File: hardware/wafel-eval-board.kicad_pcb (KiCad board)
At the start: 2 copper layers, 95 x 95 mm, 117 parts, among them U101 TPS70933, U102 LM5163DDA, U201 BQ769x2

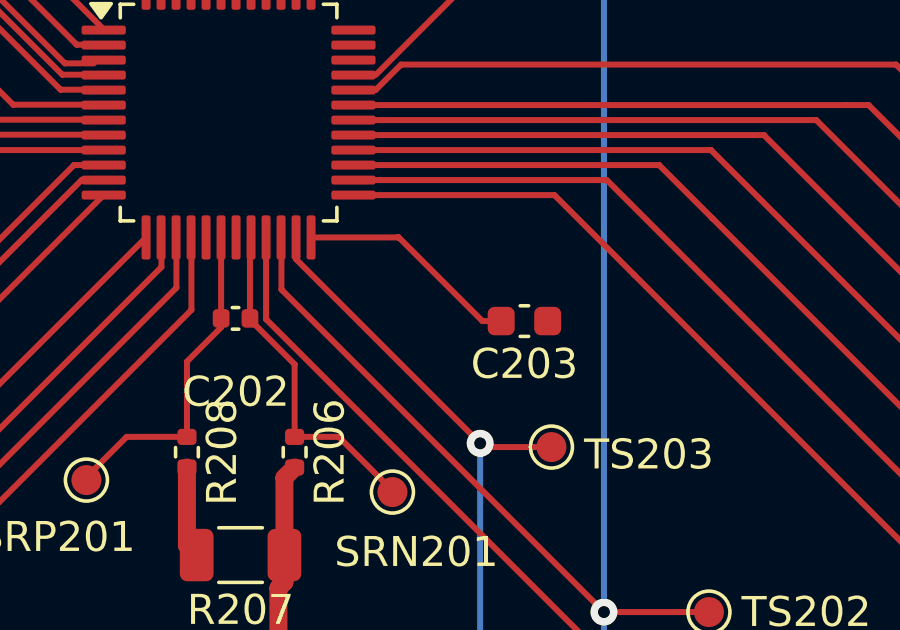
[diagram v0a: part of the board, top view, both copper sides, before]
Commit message: add sync folder
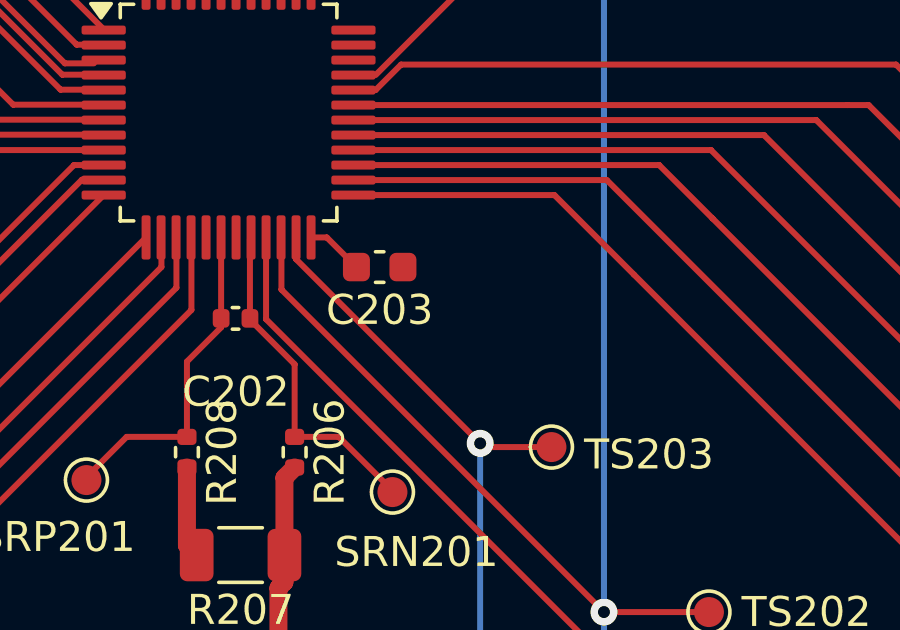
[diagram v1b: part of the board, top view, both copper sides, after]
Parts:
- moved C203 5.15 mm to (142.3, 93.0)
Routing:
- net Net-(U201-REG18): track 7.50 -> 1.92 mm
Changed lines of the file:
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@@
 	(footprint "Capacitor_SMD:C_0603_1608Metric"
 		(layer "F.Cu")
-		(at 147.1 94.8 180)
+		(at 142.275 93 180)
 		(descr "Capacitor SMD 0603 (1608 Metric), square (rectangular) end terminal, IPC-7351 nominal, (Body size source: IPC-SM-782 page 76, https://www.pcb-3d.com/wordpress/wp-content/uploads/ipc-sm-782a_amendment_1_and_2.pdf), generated with kicad-footprint-generator")
 		(tags "capacitor")
@@
 	)
 	(segment
-		(start 142.9 92)
-		(end 145.7 94.8)
+		(start 140.5125 92.0125)
+		(end 141.5 93)
 		(width 0.2)
 		(layer "F.Cu")
@@
 	(segment
 		(start 139.9875 92.0125)
-		(end 142.8875 92.0125)
-		(width 0.2)
-		(layer "F.Cu")
-		(net 14)
-	)
-	(segment
-		(start 142.8875 92.0125)
-		(end 142.9 92)
-		(width 0.2)
-		(layer "F.Cu")
-		(net 14)
-	)
-	(segment
-		(start 145.7 94.8)
-		(end 146.325 94.8)
+		(end 140.5125 92.0125)
 		(width 0.2)
 		(layer "F.Cu")

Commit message: update schematics
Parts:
- removed +3.3V101, EN101, TS201, TS202, TS203: TestPoint, TestPoint:TestPoint_Pad_D1.0mm
- removed C112, C215, C216, C217, C218, C219, C220, C221, C222: 100n, Capacitor_SMD:C_0402_1005Metric
- removed FB101, FB102, FB103, FB104: BLM18KG471SN1D, Samacsys:BLM18SP221SN1B
- removed JP201, JP202, JP203, JP204, JP205, JP206, JP207, JP208, JP209, JP210, JP211, JP212, JP213: Cell_shunt, Jumper:SolderJumper-2_P1.3mm_Open_Pad1.0x1.5mm
- removed J_BAT101: 395443018, Snapeda:CONN_SD-39544-001_NONE_18P_MOL
- removed J_GTS101: FET Gates, Connector_JST:JST_EH_B10B-EH-A_1x10_P2.50mm_Vertical
- removed J_JMPR101: EN TS1 TS3, Connector_JST:JST_EH_B10B-EH-A_1x10_P2.50mm_Vertical
- removed J_MCU101: Digital, Connector_JST:JST_EH_B10B-EH-A_1x10_P2.50mm_Vertical
- removed R110: 523k, Resistor_SMD:R_0402_1005Metric
- removed R111: 200k, Resistor_SMD:R_0402_1005Metric
- removed R112: 63.4k, Resistor_SMD:R_0402_1005Metric
- removed R113, R114, R115, R116, R117, R204: 5.1k, Resistor_SMD:R_0402_1005Metric
- removed R213, R214, R215, R216, R217, R218, R219, R220, R221, R222, R223, R224, R225, R226: 56, Resistor_SMD:R_1206_3216Metric
- removed U102: LM5163DDA, Package_SO:HSOP-8-1EP_3.9x4.9mm_P1.27mm_EP2.41x3.1mm_ThermalVias
- added C301: 0.1u, Capacitor_SMD:C_0805_2012Metric, F.Cu at (208.7, 89.4)
- added C302: 0.1u, Capacitor_SMD:C_0805_2012Metric, F.Cu at (208.7, 92.4)
- added C303: 0.1u, Capacitor_SMD:C_0805_2012Metric, F.Cu at (208.7, 95.4)
- added C304: 0.1u, Capacitor_SMD:C_0805_2012Metric, F.Cu at (208.7, 98.5)
- added C305: 0.1u, Capacitor_SMD:C_0805_2012Metric, F.Cu at (208.7, 101.5)
- added C306: 0.1u, Capacitor_SMD:C_0805_2012Metric, F.Cu at (208.7, 104.5)
- added C801: 470u, Capacitor_SMD:C_0805_2012Metric, F.Cu at (213.1, 117.4)
- added C802: 0.1u, Capacitor_SMD:C_0805_2012Metric, F.Cu at (213.1, 120.4)
- added C803: 0.1u, Capacitor_SMD:C_0805_2012Metric, F.Cu at (213.1, 123.4)
- added C804: 4.7n, Capacitor_SMD:C_0805_2012Metric, F.Cu at (213.1, 126.5)
- added C805: 0.1u, Capacitor_SMD:C_0805_2012Metric, F.Cu at (213.1, 129.5)
- added C901: 220n, Capacitor_SMD:C_0805_2012Metric, F.Cu at (241.6, 109.7)
- added C902: 220n, Capacitor_SMD:C_0805_2012Metric, F.Cu at (241.6, 112.7)
- added C903: 220n, Capacitor_SMD:C_0805_2012Metric, F.Cu at (241.6, 115.7)
- added C904: 220n, Capacitor_SMD:C_0805_2012Metric, F.Cu at (241.6, 118.7)
- added C905: 220n, Capacitor_SMD:C_0805_2012Metric, F.Cu at (246.1, 109.7)
- added C906: 220n, Capacitor_SMD:C_0805_2012Metric, F.Cu at (246.1, 112.7)
- added C907: 220n, Capacitor_SMD:C_0805_2012Metric, F.Cu at (246.1, 115.7)
- added C908: 220n, Capacitor_SMD:C_0805_2012Metric, F.Cu at (246.1, 118.7)
- added C909: 220n, Capacitor_SMD:C_0805_2012Metric, F.Cu at (250.5, 109.7)
- added C910: 220n, Capacitor_SMD:C_0805_2012Metric, F.Cu at (250.5, 112.7)
- added C911: 220n, Capacitor_SMD:C_0805_2012Metric, F.Cu at (250.5, 115.7)
- added C912: 220n, Capacitor_SMD:C_0805_2012Metric, F.Cu at (250.5, 118.7)
- added CP202: TestPoint, TestPoint:TestPoint_Pad_D1.0mm, F.Cu at (137.9, 84.1)
- added D202: BAT54SDW, Package_TO_SOT_SMD:SOT-363_SC-70-6, F.Cu at (249.8, 103.2)
- added D301: SMBJ70A, Diode_SMD:D_SMB, F.Cu at (114.5, 146.5)
- added D303: BAT46, Diode_THT:D_DO-35_SOD27_P7.62mm_Horizontal, F.Cu at (212.5, 89.7)
- added D304: 1N4148W, Diode_SMD:D_SOD-123, F.Cu at (230.1, 89.6)
- added D305: BZT52B82, Diode_SMD:D_SOD-123F, F.Cu at (224.5, 89.6)
- added D306: BZT52Bxx, Diode_SMD:D_SOD-123F, F.Cu at (224.5, 92.9)
- added D307: 1N4148W, Diode_SMD:D_SOD-123, F.Cu at (230.1, 92.9)
- added D308: BZT52B82, Diode_SMD:D_SOD-123F, F.Cu at (224.5, 96.3)
- added D309: BZT52B82, Diode_SMD:D_SOD-123F, F.Cu at (224.5, 99.6)
- added D310: BAT46, Diode_THT:D_DO-35_SOD27_P7.62mm_Horizontal, F.Cu at (212.5, 93.2)
- added D311: BAT46, Diode_THT:D_DO-35_SOD27_P7.62mm_Horizontal, F.Cu at (212.5, 96.8)
- added D312: BAT46, Diode_THT:D_DO-35_SOD27_P7.62mm_Horizontal, F.Cu at (212.5, 100.3)
- added D401: BZT52B16, Diode_SMD:D_SOD-123F, F.Cu at (268.7, 58.0)
- added D501: BZT52B16, Diode_SMD:D_SOD-123F, F.Cu at (293.9, 58.0)
- added D601: BZT52B75, Diode_SMD:D_SOD-123F, F.Cu at (264.0, 97.8)
- added D602: BZT52B16, Diode_SMD:D_SOD-123F, F.Cu at (264.0, 101.1)
- added D701: BZT52B75, Diode_SMD:D_SOD-123F, F.Cu at (242.2, 135.5)
- added D702: BZT52B16, Diode_SMD:D_SOD-123F, F.Cu at (242.2, 138.8)
- added D801: NUP2105L, Package_TO_SOT_SMD:SOT-23, F.Cu at (228.6, 133.4)
- added D802: ESD2CAN24-Q1, Package_TO_SOT_SMD:SOT-23, F.Cu at (228.6, 137.9)
- added D901: BZT52C3V6, Diode_SMD:D_SOD-123, F.Cu at (242.3, 121.9)
- added F101: 0.2A, Fuse:Fuse_Littelfuse-NANO2-451_453, F.Cu at (235.0, 70.7)
- added F102: 25A, Fuse:Fuse_Littelfuse-NANO2-451_453, F.Cu at (235.0, 75.4)
- added F801: 0.1A, Fuse:Fuse_Littelfuse-NANO2-451_453, F.Cu at (219.6, 124.1)
- added F802: 0.2A, Fuse:Fuse_Littelfuse-NANO2-451_453, F.Cu at (219.6, 128.8)
- added H102: CELL7, MountingHole:MountingHole_3.2mm_M3_Pad, F.Cu at (87.7, 106.5)
- added H103: CELL5, MountingHole:MountingHole_3.2mm_M3_Pad, F.Cu at (104.1, 106.5)
- added H104: CELL3, MountingHole:MountingHole_3.2mm_M3_Pad, F.Cu at (120.6, 106.5)
- added H105: CELL1, MountingHole:MountingHole_3.2mm_M3_Pad, F.Cu at (137.0, 106.5)
- added H106: BAT-, MountingHole:MountingHole_3.2mm_M3_Pad, F.Cu at (153.5, 106.5)
- added H107: CELL10, MountingHole:MountingHole_3.2mm_M3_Pad, F.Cu at (63.0, 106.5)
- added H108: CELL8, MountingHole:MountingHole_3.2mm_M3_Pad, F.Cu at (79.5, 106.5)
- added H109: CELL6, MountingHole:MountingHole_3.2mm_M3_Pad, F.Cu at (95.9, 106.5)
- added H110: CELL4, MountingHole:MountingHole_3.2mm_M3_Pad, F.Cu at (112.4, 106.5)
- added H111: CELL2, MountingHole:MountingHole_3.2mm_M3_Pad, F.Cu at (128.8, 106.5)
- added H112: CELL0, MountingHole:MountingHole_3.2mm_M3_Pad, F.Cu at (145.3, 106.5)
- added H113: PACK+, MountingHole:MountingHole_3.2mm_M3_Pad, F.Cu at (63.0, 77.0)
- added H114: PACK-, MountingHole:MountingHole_3.2mm_M3_Pad, F.Cu at (63.0, 67.5)
- added H115: CH, MountingHole:MountingHole_3.2mm_M3_Pad, F.Cu at (63.0, 58.0)
- added J101: CAN PORT, Connector_JST:JST_PH_S4B-PH-K_1x04_P2.00mm_Horizontal, F.Cu at (221.8, 70.7)
- added J102: SW, Connector_JST:JST_PH_S2B-PH-K_1x02_P2.00mm_Horizontal, F.Cu at (213.9, 70.7)
- added J801: UART1, Connector_JST:JST_EH_B3B-EH-A_1x03_P2.50mm_Vertical, F.Cu at (218.9, 118.5)
- added L102: 68u, Inductor_SMD:L_KOHERelec_MDA7030, F.Cu at (142.3, 65.1)
- added Q1001: DMG2302UK, Package_TO_SOT_SMD:SOT-23, F.Cu at (263.7, 107.0)
- added Q1101: DMG2302UK, Package_TO_SOT_SMD:SOT-23, F.Cu at (286.3, 134.6)
- added Q1201: DMG2302UK, Package_TO_SOT_SMD:SOT-23, F.Cu at (275.0, 120.8)
- added Q1301: DMG2302UK, Package_TO_SOT_SMD:SOT-23, F.Cu at (286.3, 120.8)
- added Q1401: DMG2302UK, Package_TO_SOT_SMD:SOT-23, F.Cu at (286.3, 107.0)
- added Q1501: DMG2302UK, Package_TO_SOT_SMD:SOT-23, F.Cu at (275.0, 107.0)
- added Q1601: DMG2302UK, Package_TO_SOT_SMD:SOT-23, F.Cu at (282.3, 90.1)
- added Q1701: DMG2302UK, Package_TO_SOT_SMD:SOT-23, F.Cu at (263.7, 134.6)
- added Q1801: DMG2302UK, Package_TO_SOT_SMD:SOT-23, F.Cu at (275.0, 134.6)
- added Q1901: DMG2302UK, Package_TO_SOT_SMD:SOT-23, F.Cu at (263.7, 120.8)
- added Q2001: DMG2302UK, Package_TO_SOT_SMD:SOT-23, F.Cu at (293.6, 90.1)
- added Q201: NPN, Package_TO_SOT_SMD:SOT-23, F.Cu at (112.7, 153.5)
- added Q202: 2N7002, Package_TO_SOT_SMD:SOT-23, F.Cu at (250.3, 99.2)
- added Q301: IRLML6402, Package_TO_SOT_SMD:SOT-23, F.Cu at (226.6, 104.3)
- added Q302: 2N7002, Package_TO_SOT_SMD:SOT-23, F.Cu at (226.6, 108.8)
- added Q401: IPB085N15NM6, Package_TO_SOT_SMD:TO-263-2, F.Cu at (259.0, 50.7)
- added Q402: IPB085N15NM6, Package_TO_SOT_SMD:TO-263-2, F.Cu at (259.0, 63.0)
- added Q403: IPB085N15NM6, Package_TO_SOT_SMD:TO-263-2, F.Cu at (259.0, 75.4)
- added Q501: IPB085N15NM6, Package_TO_SOT_SMD:TO-263-2, F.Cu at (284.2, 50.7)
- added Q502: IPB085N15NM6, Package_TO_SOT_SMD:TO-263-2, F.Cu at (284.2, 63.0)
- added Q503: IPB085N15NM6, Package_TO_SOT_SMD:TO-263-2, F.Cu at (284.2, 75.4)
- added Q601: PMOS, Package_TO_SOT_SMD:TO-252-3_TabPin2, F.Cu at (268.2, 92.1)
- added Q701: PMOS, Package_TO_SOT_SMD:TO-252-3_TabPin2, F.Cu at (246.3, 129.8)
- added R1001: 100R 1206, Resistor_SMD:R_0805_2012Metric, F.Cu at (259.0, 106.3)
- added R1002: 100R 1206, Resistor_SMD:R_0805_2012Metric, F.Cu at (259.0, 109.2)
- added R1003: 10k 0603, Resistor_SMD:R_0805_2012Metric, F.Cu at (259.0, 112.2)
- added R1004: 100R 0603, Resistor_SMD:R_0805_2012Metric, F.Cu at (259.0, 115.1)
- added R1101: 100R 1206, Resistor_SMD:R_0805_2012Metric, F.Cu at (281.7, 133.9)
- added R1102: 100R 1206, Resistor_SMD:R_0805_2012Metric, F.Cu at (281.7, 136.8)
- added R1103: 10k 0603, Resistor_SMD:R_0805_2012Metric, F.Cu at (281.7, 139.8)
- added R1104: 100R 0603, Resistor_SMD:R_0805_2012Metric, F.Cu at (281.7, 142.7)
- added R1201: 100R 1206, Resistor_SMD:R_0805_2012Metric, F.Cu at (270.4, 120.1)
- added R1202: 100R 1206, Resistor_SMD:R_0805_2012Metric, F.Cu at (270.4, 123.0)
- added R1203: 10k 0603, Resistor_SMD:R_0805_2012Metric, F.Cu at (270.4, 126.0)
- added R1204: 100R 0603, Resistor_SMD:R_0805_2012Metric, F.Cu at (270.4, 128.9)
- added R1301: 100R 1206, Resistor_SMD:R_0805_2012Metric, F.Cu at (281.7, 120.1)
- added R1302: 100R 1206, Resistor_SMD:R_0805_2012Metric, F.Cu at (281.7, 123.0)
- added R1303: 10k 0603, Resistor_SMD:R_0805_2012Metric, F.Cu at (281.7, 126.0)
- added R1304: 100R 0603, Resistor_SMD:R_0805_2012Metric, F.Cu at (281.7, 128.9)
- added R1401: 100R 1206, Resistor_SMD:R_0805_2012Metric, F.Cu at (281.7, 106.3)
- added R1402: 100R 1206, Resistor_SMD:R_0805_2012Metric, F.Cu at (281.7, 109.2)
- added R1403: 10k 0603, Resistor_SMD:R_0805_2012Metric, F.Cu at (281.7, 112.2)
- added R1404: 100R 0603, Resistor_SMD:R_0805_2012Metric, F.Cu at (281.7, 115.1)
- added R1501: 100R 1206, Resistor_SMD:R_0805_2012Metric, F.Cu at (270.4, 106.3)
- added R1502: 100R 1206, Resistor_SMD:R_0805_2012Metric, F.Cu at (270.4, 109.2)
- added R1503: 10k 0603, Resistor_SMD:R_0805_2012Metric, F.Cu at (270.4, 112.2)
- added R1504: 100R 0603, Resistor_SMD:R_0805_2012Metric, F.Cu at (270.4, 115.1)
- added R1601: 100R 1206, Resistor_SMD:R_0805_2012Metric, F.Cu at (277.6, 89.4)
- added R1602: 100R 1206, Resistor_SMD:R_0805_2012Metric, F.Cu at (277.6, 92.3)
- added R1603: 10k 0603, Resistor_SMD:R_0805_2012Metric, F.Cu at (277.6, 95.3)
- added R1604: 100R 0603, Resistor_SMD:R_0805_2012Metric, F.Cu at (277.6, 98.2)
- added R1701: 100R 1206, Resistor_SMD:R_0805_2012Metric, F.Cu at (259.0, 133.9)
- added R1702: 100R 1206, Resistor_SMD:R_0805_2012Metric, F.Cu at (259.0, 136.8)
- added R1703: 10k 0603, Resistor_SMD:R_0805_2012Metric, F.Cu at (259.0, 139.8)
- added R1704: 100R 0603, Resistor_SMD:R_0805_2012Metric, F.Cu at (259.0, 142.7)
- added R1801: 100R 1206, Resistor_SMD:R_0805_2012Metric, F.Cu at (270.4, 133.9)
- added R1802: 100R 1206, Resistor_SMD:R_0805_2012Metric, F.Cu at (270.4, 136.8)
- added R1803: 10k 0603, Resistor_SMD:R_0805_2012Metric, F.Cu at (270.4, 139.8)
- added R1804: 100R 0603, Resistor_SMD:R_0805_2012Metric, F.Cu at (270.4, 142.7)
- added R1901: 100R 1206, Resistor_SMD:R_0805_2012Metric, F.Cu at (259.0, 120.1)
- added R1902: 100R 1206, Resistor_SMD:R_0805_2012Metric, F.Cu at (259.0, 123.0)
- added R1903: 10k 0603, Resistor_SMD:R_0805_2012Metric, F.Cu at (259.0, 126.0)
- added R1904: 100R 0603, Resistor_SMD:R_0805_2012Metric, F.Cu at (259.0, 128.9)
- added R2001: 100R 1206, Resistor_SMD:R_0805_2012Metric, F.Cu at (288.9, 89.4)
- added R2002: 100R 1206, Resistor_SMD:R_0805_2012Metric, F.Cu at (288.9, 92.3)
- added R2003: 10k 0603, Resistor_SMD:R_0805_2012Metric, F.Cu at (288.9, 95.3)
- added R2004: 100R 0603, Resistor_SMD:R_0805_2012Metric, F.Cu at (288.9, 98.2)
- added R301: 100, Resistor_SMD:R_0805_2012Metric, F.Cu at (213.2, 103.6)
- added R302: 100, Resistor_SMD:R_0805_2012Metric, F.Cu at (213.2, 106.5)
- added R303: 5.1K, Resistor_SMD:R_0805_2012Metric, F.Cu at (213.2, 109.5)
- added R304: 5.1K, Resistor_SMD:R_0805_2012Metric, F.Cu at (213.2, 112.4)
- added R305: 511, Resistor_SMD:R_0805_2012Metric, F.Cu at (217.6, 103.6)
- added R306: 10M, Resistor_SMD:R_0805_2012Metric, F.Cu at (217.6, 106.5)
- added R307: 10M, Resistor_SMD:R_0805_2012Metric, F.Cu at (217.6, 109.5)
- added R308: 5.1k, Resistor_SMD:R_0805_2012Metric, F.Cu at (217.6, 112.4)
- added R309: 49.9k, Resistor_SMD:R_0805_2012Metric, F.Cu at (222.0, 103.6)
- added R310: 49.9k, Resistor_SMD:R_0805_2012Metric, F.Cu at (222.0, 106.5)
- added R311: 20k, Resistor_SMD:R_0805_2012Metric, F.Cu at (222.0, 109.5)
- added R312: 20k, Resistor_SMD:R_0805_2012Metric, F.Cu at (222.0, 112.4)
- added R401: 10M, Resistor_SMD:R_0805_2012Metric, F.Cu at (268.2, 46.0)
- added R402: 51, Resistor_SMD:R_0805_2012Metric, F.Cu at (268.2, 48.9)
- added R403: 51, Resistor_SMD:R_0805_2012Metric, F.Cu at (268.2, 51.9)
- added R404: 51, Resistor_SMD:R_0805_2012Metric, F.Cu at (268.2, 54.8)
- added R501: 10M, Resistor_SMD:R_0805_2012Metric, F.Cu at (293.3, 46.0)
- added R502: 51, Resistor_SMD:R_0805_2012Metric, F.Cu at (293.3, 48.9)
- added R503: 51, Resistor_SMD:R_0805_2012Metric, F.Cu at (293.3, 51.9)
- added R504: 51, Resistor_SMD:R_0805_2012Metric, F.Cu at (293.3, 54.8)
- added R601: 51, Resistor_SMD:R_0805_2012Metric, F.Cu at (259.0, 89.4)
- added R602: 1M, Resistor_SMD:R_0805_2012Metric, F.Cu at (259.0, 92.3)
- added R603: 510, Resistor_SMD:R_0805_2012Metric, F.Cu at (259.0, 95.3)
- added R604: 510, Resistor_SMD:R_0805_2012Metric, F.Cu at (259.0, 98.2)
- added R701: 51, Resistor_SMD:R_0805_2012Metric, F.Cu at (237.2, 127.1)
- added R702: 1M, Resistor_SMD:R_0805_2012Metric, F.Cu at (237.2, 130.0)
- added R703: 510, Resistor_SMD:R_0805_2012Metric, F.Cu at (237.2, 133.0)
- added R704: 510, Resistor_SMD:R_0805_2012Metric, F.Cu at (237.2, 135.9)
- added R801: 100, Resistor_SMD:R_0805_2012Metric, F.Cu at (208.7, 117.4)
- added R802: 100, Resistor_SMD:R_0805_2012Metric, F.Cu at (208.7, 120.3)
- added R803: 100, Resistor_SMD:R_0805_2012Metric, F.Cu at (208.7, 123.3)
- added R804: 60.4, Resistor_SMD:R_0805_2012Metric, F.Cu at (208.7, 126.2)
- added R805: 60.4, Resistor_SMD:R_0805_2012Metric, F.Cu at (208.7, 129.2)
- added R806: 100, Resistor_SMD:R_0805_2012Metric, F.Cu at (208.7, 132.1)
- added R807: 0, Resistor_SMD:R_0805_2012Metric, F.Cu at (208.7, 135.1)
- added R901: 100, Resistor_SMD:R_0805_2012Metric, F.Cu at (237.2, 109.7)
- added R902: 100, Resistor_SMD:R_0805_2012Metric, F.Cu at (237.2, 112.6)
- added R903: 100, Resistor_SMD:R_0805_2012Metric, F.Cu at (237.2, 115.6)
- added R904: 100, Resistor_SMD:R_0805_2012Metric, F.Cu at (237.2, 118.5)
- added R905: 100, Resistor_SMD:R_0805_2012Metric, F.Cu at (237.2, 121.5)
- added SW801: SW_Push, Button_Switch_SMD:SW_SPST_PTS810, F.Cu at (227.2, 124.1)
- added U801: NUCLEO-L432KC, wafel-eval-board:MODULE_NUCLEO-L432KC, F.Cu at (98.2, 161.9)
- added U804: TLP241A, Package_DIP:DIP-4_W7.62mm, F.Cu at (216.9, 133.2)
- added Z301: ES3D, Diode_SMD:D_SMC, F.Cu at (115.7, 139.9)
- C101, C102: value 1u -> 4.7u; footprint Capacitor_SMD:C_0402_1005Metric -> Capacitor_SMD:C_1206_3216Metric
- C103: value 1u -> 2.2u; footprint Capacitor_SMD:C_0402_1005Metric -> Capacitor_SMD:C_1206_3216Metric
- C104: value 2.2u -> 100n
- C105: value 100n -> 2.2n; footprint Capacitor_SMD:C_1206_3216Metric -> Capacitor_SMD:C_0805_2012Metric
- C106: value 2.2n -> 100p; footprint Capacitor_SMD:C_0402_1005Metric -> Capacitor_SMD:C_0805_2012Metric
- C107: value 100p -> NC; footprint Capacitor_SMD:C_0603_1608Metric -> Capacitor_SMD:C_0805_2012Metric
- C108: footprint Capacitor_SMD:C_0603_1608Metric -> Capacitor_SMD:C_0805_2012Metric
- C109, C110, C111: footprint Capacitor_SMD:C_0805_2012Metric -> Capacitor_SMD:C_1206_3216Metric
- C201: value 470n -> 100p; footprint Capacitor_SMD:C_0603_1608Metric -> Capacitor_SMD:C_0805_2012Metric
- C202: value 100n -> 1u; footprint Capacitor_SMD:C_0402_1005Metric -> Capacitor_SMD:C_1206_3216Metric
- C203: value 2.2u -> 1u; footprint Capacitor_SMD:C_0603_1608Metric -> Capacitor_SMD:C_0805_2012Metric
- C204: value 100p -> 1u; footprint Capacitor_SMD:C_0603_1608Metric -> Capacitor_SMD:C_0805_2012Metric
- C205: value 1u -> 470n; footprint Capacitor_SMD:C_1206_3216Metric -> Capacitor_SMD:C_0805_2012Metric
- C206: value 100n -> 100p; footprint Capacitor_SMD:C_0402_1005Metric -> Capacitor_SMD:C_0805_2012Metric
- C207, C209: value 100n -> 1u; footprint Capacitor_SMD:C_0402_1005Metric -> Capacitor_SMD:C_0805_2012Metric
- C208: value 100n -> 2.2u; footprint Capacitor_SMD:C_0402_1005Metric -> Capacitor_SMD:C_1206_3216Metric
- C210, C211, C212, C213, C214: value 100n -> 470p; footprint Capacitor_SMD:C_0402_1005Metric -> Capacitor_SMD:C_0805_2012Metric
- D101: value DF5A5.6LFU -> SS110; footprint Samacsys:SSOP5-P-0.65A -> Diode_SMD:D_SMA
- D102: value DF5A5.6LFU -> LED; footprint Samacsys:SSOP5-P-0.65A -> LED_THT:LED_D3.0mm
- D201: value LED -> SS110; footprint LED_THT:LED_D3.0mm -> Diode_SMD:D_SMA
- F201: value 20A -> 0.1A
- H101: value PACK- -> CELL9
- L101: value 68u -> 10u
- R101: value 120 -> 100; footprint Resistor_SMD:R_0402_1005Metric -> Resistor_SMD:R_0805_2012Metric
- R102, R208: footprint Resistor_SMD:R_0402_1005Metric -> Resistor_SMD:R_0805_2012Metric
- R103: value 120 -> 5.1k; footprint Resistor_SMD:R_0402_1005Metric -> Resistor_SMD:R_0805_2012Metric
- R104: value 120 -> 82.5K; footprint Resistor_SMD:R_0402_1005Metric -> Resistor_SMD:R_0805_2012Metric
- R105, R106: value 120 -> 0; footprint Resistor_SMD:R_0402_1005Metric -> Resistor_SMD:R_0805_2012Metric
- R107: value 120 -> 523K; footprint Resistor_SMD:R_0402_1005Metric -> Resistor_SMD:R_0805_2012Metric
- R108: value 120 -> 200K; footprint Resistor_SMD:R_0402_1005Metric -> Resistor_SMD:R_0805_2012Metric
- R109: value 82.5k -> 63.4k; footprint Resistor_SMD:R_0402_1005Metric -> Resistor_SMD:R_0805_2012Metric
- R201: value 5.1k -> 10k; footprint Resistor_SMD:R_0402_1005Metric -> Resistor_SMD:R_0805_2012Metric
- R202, R205: value 5.1k -> 10K; footprint Resistor_SMD:R_0402_1005Metric -> Resistor_SMD:R_0805_2012Metric
- R203: value 5.1k -> 120; footprint Resistor_SMD:R_0402_1005Metric -> Resistor_SMD:R_0805_2012Metric
- R206: value 120 -> 10M; footprint Resistor_SMD:R_0402_1005Metric -> Resistor_SMD:R_0805_2012Metric
- R207: value 0.2m -> 100; footprint Resistor_SMD:R_1206_3216Metric -> Resistor_SMD:R_0805_2012Metric
- R209: value 120 -> 50k; footprint Resistor_SMD:R_0402_1005Metric -> Resistor_SMD:R_0805_2012Metric
- R210, R212: value 56 -> 120; footprint Resistor_SMD:R_1206_3216Metric -> Resistor_SMD:R_0805_2012Metric
- R211: value 56 -> 1m
- U101: value TPS70933 -> LM5163DDA; footprint Package_TO_SOT_SMD:SOT-23-5 -> Package_SO:HSOP-8-1EP_3.9x4.9mm_P1.27mm_EP2.41x3.1mm_ThermalVias
- U201: value BQ769x2 -> BQ7694204
- moved F201 138.5 mm to (243.6, 99.3)
- moved C212 133.0 mm to (250.5, 89.4), turned to 0 degrees
- moved C213 132.7 mm to (250.5, 92.4), turned to 0 degrees
- moved C214 132.6 mm to (250.5, 95.4), turned to 0 degrees
- moved C209 130.1 mm to (246.1, 89.4), turned to 0 degrees
- moved C210 130.0 mm to (246.1, 92.4), turned to 0 degrees
- moved C207 129.8 mm to (241.6, 95.4), turned to 0 degrees
- moved C211 129.6 mm to (246.1, 95.4), turned to 0 degrees
- moved CP201 123.1 mm to (253.3, 102.9)
- moved R209 116.0 mm to (237.2, 104.1), turned to 0 degrees
- moved C204 112.3 mm to (241.6, 92.4)
- moved D201 107.1 mm to (243.5, 103.9), turned to 0 degrees
- moved R205 106.1 mm to (237.2, 92.3), turned to 0 degrees
- moved R208 101.4 mm to (237.2, 101.2), turned to 0 degrees
- moved R207 99.7 mm to (237.2, 98.2), turned to 0 degrees
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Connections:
- C101 pad 1: +5V -> GND
- C101 pad 2: GND -> Net-(D101-K)
- C102 pad 1: +3.3V -> GND
- C102 pad 2: GND -> Net-(C102-Pad2)
- C103 pad 1: +3.3V -> GND
- C103 pad 2: GND -> Net-(U101-EN/UVLO)
- C104 pad 1: GND -> Net-(U101-EN/UVLO)
- C104 pad 2: /BAT+ -> GND
- C105 pad 1: /BAT+ -> Net-(C105-Pad1)
- C105 pad 2: GND -> Net-(U101-SW)
- C106 pad 1: Net-(U102-BST) -> Net-(C106-Pad1)
- C106 pad 2: Net-(U102-SW) -> Net-(U101-FB)
- C107 pad 2: Net-(U102-FB) -> GND
- C108 pad 1: Net-(C107-Pad1) -> Net-(C106-Pad1)
- C201 pad 2: Net-(U201-CP1) -> GND
- C202 pad 1: Net-(U201-SRN) -> /Frontend/BAT
- C202 pad 2: Net-(U201-SRP) -> GND
- C203 pad 2: Net-(U201-REG18) -> Net-(Q201-E)
- C204 pad 1: /Frontend/BAT -> Net-(U201-SRN)
- C205 pad 2: GND -> Net-(U201-CP1)
- C206 pad 1: Net-(U201-VC16) -> Net-(U201-SRN)
- C206 pad 2: Net-(JP201-B) -> Net-(U201-SRP)
- C207 pad 1: Net-(JP201-B) -> Net-(U201-SRN)
- C207 pad 2: Net-(JP201-A) -> Net-(U201-SRP)
- C208 pad 1: Net-(JP201-A) -> GND
- C208 pad 2: Net-(JP202-A) -> Net-(U201-REG18)
- C209 pad 1: Net-(JP202-A) -> Net-(U201-SRP)
- C209 pad 2: Net-(JP203-A) -> GND
- C210 pad 1: Net-(JP203-A) -> /Frontend/TS1
- C210 pad 2: Net-(JP204-A) -> GND
- C211 pad 1: Net-(JP204-A) -> /Frontend/TS2
- C211 pad 2: Net-(JP205-A) -> GND
- C212 pad 1: Net-(JP205-A) -> /Frontend/TS3
- C212 pad 2: Net-(JP206-A) -> GND
- C213 pad 1: Net-(JP206-A) -> /Frontend/TS4
- C213 pad 2: Net-(JP207-A) -> GND
- C214 pad 1: Net-(JP207-A) -> /Frontend/TS5
- C214 pad 2: Net-(JP208-A) -> GND
- CP201 pad 1: Net-(U201-CP1) -> Net-(Q201-E)
- D101 pad 1: /xHDQ -> Net-(D101-K)
- D101 pad 2: GND -> Net-(D101-A)
- D102 pad 1: /xDDSG -> Net-(D102-K)
- D102 pad 2: GND -> Net-(D102-A)
- D201 pad 1: GND -> Net-(D201-K)
- D201 pad 2: Net-(D201-A) -> /CB Mosfets/VC10
- F201 pad 1: /Frontend/CELL17 -> Net-(D202A-K)
- F201 pad 2: /BAT+ -> Net-(U201-REG1)
- H101 pad 1: /Frontend/PACK- -> /CB Mosfets/CELL9
- L101 pad 1: Net-(U102-SW) -> Net-(D101-K)
- L101 pad 2: +5V -> Net-(C102-Pad2)
- R101 pad 1: /xALERT -> Net-(C102-Pad2)
- R101 pad 2: /Frontend/ALERT -> Net-(U101-EN/UVLO)
- R102 pad 1: /xSCL -> Net-(F103-Pad2)
- R102 pad 2: /Frontend/SCL -> Net-(Q101-D)
- R103 pad 1: /xSDA -> GND
- R103 pad 2: /Frontend/SDA -> Net-(D102-K)
- R104 pad 1: /xHDQ -> Net-(U101-RON)
- R104 pad 2: /Frontend/HDQ -> GND
- R105 pad 1: /xCFETOFF -> Net-(U101-BST)
- R105 pad 2: /Frontend/CFETOFF -> Net-(C105-Pad1)
- R106 pad 1: /xDFETOFF -> Net-(U101-SW)
- R106 pad 2: /Frontend/DFETOFF -> Net-(C107-Pad1)
- R107 pad 1: /xDCHG -> Net-(U101-SW)
- R107 pad 2: /Frontend/DCHG -> Net-(C106-Pad1)
- R108 pad 1: /xDDSG -> +5V
- R108 pad 2: /Frontend/DDSG -> Net-(U101-FB)
- R109 pad 1: Net-(U102-RON) -> Net-(U101-FB)
- R202 pad 1: unconnected-(R202-Pad1) -> /Frontend/SPI.CS
- R202 pad 2: /EN -> +3.3V
- R203 pad 1: /Frontend/FUSE -> /Frontend/BAT
- R203 pad 2: Net-(D201-A) -> /BAT+
- R205 pad 1: /BAT+ -> /Frontend/ALERT
- R205 pad 2: Net-(U201-LD) -> +3.3V
- R206 pad 1: Net-(U201-SRN) -> GND
- R206 pad 2: /Frontend/PACK- -> Net-(Q201-B)
- R207 pad 1: /Frontend/PACK- -> Net-(U201-BREG)
- R207 pad 2: GND -> Net-(Q201-B)
- R208 pad 1: Net-(U201-SRP) -> Net-(Q202-G)
- R208 pad 2: GND -> /Frontend/WAKE
- R209 pad 1: /Frontend/BAT -> /Frontend/WAKE
- R209 pad 2: /BAT+ -> GND
- R210 pad 1: Net-(U201-VC16) -> Net-(U201-SRN)
- R210 pad 2: /BAT+ -> PGND
- R211 pad 1: Net-(JP201-B) -> PGND
- R211 pad 2: /Frontend/CELL16 -> GND
- R212 pad 1: Net-(JP201-A) -> Net-(U201-SRP)
- R212 pad 2: /Frontend/CELL15 -> GND
- U101 pad 1: +5V -> GND
- U101 pad 2: GND -> Net-(U101-EN/UVLO)
- U101 pad 3: +5V -> Net-(U101-EN/UVLO)
- U101 pad 4: unconnected-(U101-BP-Pad4) -> Net-(U101-RON)
- U101 pad 5: +3.3V -> Net-(U101-FB)
- U201 pad 1: Net-(JP201-B) -> unconnected-(U201-VC15-Pad1)
- U201 pad 10: Net-(JP209-A) -> /CB Mosfets/VC6
- U201 pad 11: Net-(JP210-A) -> /CB Mosfets/VC5
- U201 pad 12: Net-(JP211-A) -> /CB Mosfets/VC4
- U201 pad 13: Net-(JP212-A) -> /CB Mosfets/VC3
- U201 pad 14: Net-(JP213-A) -> /CB Mosfets/VC2
- U201 pad 15: Net-(U201-VC1) -> /CB Mosfets/VC1
- U201 pad 16: Net-(U201-VC0) -> /CB Mosfets/VC0
- U201 pad 2: Net-(JP201-A) -> unconnected-(U201-VC14-Pad2)
- U201 pad 21: /TS1 -> /Frontend/TS1
- U201 pad 22: /EN -> Net-(Q202-D)
- U201 pad 23: /TS3 -> /Frontend/TS2
- U201 pad 26: /Frontend/SCL -> /Frontend/SPI.SCLK
- U201 pad 27: /Frontend/SDA -> /Frontend/SPI.MISO
- U201 pad 28: /Frontend/HDQ -> /Frontend/SPI.MOSI
- U201 pad 29: /Frontend/CFETOFF -> /Frontend/SPI.CS
- U201 pad 3: Net-(JP202-A) -> unconnected-(U201-VC13-Pad3)
- U201 pad 30: /Frontend/DFETOFF -> /Frontend/TS4
- U201 pad 31: /Frontend/DCHG -> /Frontend/TS3
- U201 pad 32: /Frontend/DDSG -> /Frontend/TS5
- U201 pad 34: unconnected-(U201-REG2-Pad34) -> Net-(D202C-K)
- U201 pad 35: unconnected-(U201-REG1-Pad35) -> Net-(U201-REG1)
- U201 pad 36: GND -> Net-(Q201-E)
- U201 pad 37: GND -> Net-(U201-BREG)
- U201 pad 38: /Frontend/FUSE -> /FUSE
- U201 pad 4: Net-(JP203-A) -> unconnected-(U201-VC12-Pad4)
- U201 pad 41: Net-(U201-LD) -> /Frontend/LD
- U201 pad 42: Net-(U201-PACK) -> /Frontend/PACK
- U201 pad 48: Net-(U201-VC16) -> unconnected-(U201-VC16-Pad48)
- U201 pad 5: Net-(JP204-A) -> unconnected-(U201-VC11-Pad5)
- U201 pad 6: Net-(JP205-A) -> /CB Mosfets/VC10
- U201 pad 7: Net-(JP206-A) -> /CB Mosfets/VC9
- U201 pad 8: Net-(JP207-A) -> /CB Mosfets/VC8
- U201 pad 9: Net-(JP208-A) -> /CB Mosfets/VC7
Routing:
- net /EN: track 148.4 -> 0.00 mm, vias 3 -> 0
- net +3.3V: track 99.2 -> 0.00 mm, vias 3 -> 0
- net /BAT+: track 80.1 -> 0.00 mm
- net /TS3: track 78.0 -> 0.00 mm, vias 2 -> 0
- net +5V: track 76.4 -> 0.00 mm, vias 2 -> 0
- net /TS1: track 66.5 -> 0.00 mm, vias 2 -> 0
- net /Frontend/PDSG: track 53.5 -> 0.00 mm, vias 2 -> 0
- net /Frontend/DSG: track 53.2 -> 0.00 mm, vias 2 -> 0
- net /Frontend/CHG: track 52.3 -> 0.00 mm, vias 2 -> 0
- net /Frontend/PCHG: track 52.0 -> 0.00 mm, vias 2 -> 0
- net Net-(U201-VC0): track 51.8 -> 0.00 mm
- net Net-(U201-VC1): track 47.9 -> 0.00 mm
- net Net-(JP201-A): track 47.7 -> 0.00 mm
- net Net-(JP201-B): track 46.4 -> 0.00 mm
- net Net-(JP213-A): track 44.1 -> 0.00 mm
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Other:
- board outline removed
- board text removed: "BQ76952"

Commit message: first layout
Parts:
- added D902: BAT42WS, Diode_SMD:D_SOD-323F, F.Cu at (149.2, 98.5)
- added R110: 2m, Resistor_SMD:R_0805_2012Metric, F.Cu at (130.1, 78.0)
- added R111: 2m, Resistor_SMD:R_0805_2012Metric, F.Cu at (130.1, 81.0)
- H114: moved to B.Cu
- R1001, R1002, R1101, R1102, R1201, R1202, R1301, R1302, R1401, R1402, R1501, R1502, R1601, R1602, R1701, R1702, R1801, R1802, R1901, R1902, R2001, R2002: value 100R 1206 -> 100R
- R1003, R1103, R1203, R1303, R1403, R1503, R1603, R1703, R1803, R1903, R2003: value 10k 0603 -> 10k
- R1004, R1104, R1204, R1304, R1404, R1504, R1604, R1704, R1804, R1904, R2004: value 100R 0603 -> 100R
- moved C904 340.8 mm to (-98.7, 136.5)
- moved C905 340.8 mm to (-94.2, 127.5)
- moved C906 340.8 mm to (-94.2, 130.5)
- moved C911 340.8 mm to (-89.8, 133.5)
- moved C912 340.8 mm to (-89.8, 136.5)
- moved Q1601 340.8 mm to (-58.0, 107.9)
- moved Q1701 340.8 mm to (-76.6, 152.4)
- moved Q1901 340.8 mm to (-76.6, 138.6)
- moved R1601 340.8 mm to (-62.7, 107.2)
- moved R1602 340.8 mm to (-62.7, 110.1)
- moved R1603 340.8 mm to (-62.7, 113.1)
- moved R1604 340.8 mm to (-62.7, 116.0)
- moved R1701 340.8 mm to (-81.2, 151.7)
- moved R1702 340.8 mm to (-81.2, 154.6)
- moved R1703 340.8 mm to (-81.2, 157.6)
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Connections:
- C204 pad 2: GND -> PGND

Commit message: placed c mosfet
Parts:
- removed the C906 at (-94.2, 130.5)
- removed Q2001: DMG2302UK, Package_TO_SOT_SMD:SOT-23
- removed R2001, R2002, R2004: 100R, Resistor_SMD:R_0805_2012Metric
- removed R2003: 10k, Resistor_SMD:R_0805_2012Metric
- added C912: 100n, Capacitor_SMD:C_0603_1608Metric, F.Cu at (120.4, 86.8)
- added Q901: ZXMP10A13FTA, Package_TO_SOT_SMD:SOT-23, F.Cu at (117.0, 86.1)
- added Q902: BSS123, Package_TO_SOT_SMD:SOT-23, F.Cu at (116.2, 91.0)
- added R906: 100K, Resistor_SMD:R_0603_1608Metric, F.Cu at (119.6, 92.1)
- C105, C106, C107, C108, C301, C302, C303, C304, C305, C306, C801, C802, C805, C901, C902, C903, C904, C905: footprint Capacitor_SMD:C_0805_2012Metric -> Capacitor_SMD:C_0603_1608Metric
- C202: renamed from C201; footprint Capacitor_SMD:C_0805_2012Metric -> Capacitor_SMD:C_0603_1608Metric
- C204: renamed from C203; footprint Capacitor_SMD:C_0805_2012Metric -> Capacitor_SMD:C_0603_1608Metric
- C205: renamed from C204; footprint Capacitor_SMD:C_0805_2012Metric -> Capacitor_SMD:C_0603_1608Metric
- C206: renamed from C205; footprint Capacitor_SMD:C_0805_2012Metric -> Capacitor_SMD:C_0603_1608Metric
- C207: renamed from C206; footprint Capacitor_SMD:C_0805_2012Metric -> Capacitor_SMD:C_0603_1608Metric
- C208: renamed from C207; footprint Capacitor_SMD:C_0805_2012Metric -> Capacitor_SMD:C_0603_1608Metric
- C210: renamed from C209; footprint Capacitor_SMD:C_0805_2012Metric -> Capacitor_SMD:C_0603_1608Metric
- C211: renamed from C210; footprint Capacitor_SMD:C_0805_2012Metric -> Capacitor_SMD:C_0603_1608Metric
- C212: renamed from C211; footprint Capacitor_SMD:C_0805_2012Metric -> Capacitor_SMD:C_0603_1608Metric
- C213: renamed from C212; footprint Capacitor_SMD:C_0805_2012Metric -> Capacitor_SMD:C_0603_1608Metric
- C214: renamed from C213; footprint Capacitor_SMD:C_0805_2012Metric -> Capacitor_SMD:C_0603_1608Metric
- C215: renamed from C214; footprint Capacitor_SMD:C_0805_2012Metric -> Capacitor_SMD:C_0603_1608Metric
- C803: renamed from C804; footprint Capacitor_SMD:C_0805_2012Metric -> Capacitor_SMD:C_0603_1608Metric
- C804: renamed from C803; footprint Capacitor_SMD:C_0805_2012Metric -> Capacitor_SMD:C_0603_1608Metric
- C906: renamed from C907; footprint Capacitor_SMD:C_0805_2012Metric -> Capacitor_SMD:C_0603_1608Metric
- C907: renamed from C908; footprint Capacitor_SMD:C_0805_2012Metric -> Capacitor_SMD:C_0603_1608Metric
- C908: renamed from C909; footprint Capacitor_SMD:C_0805_2012Metric -> Capacitor_SMD:C_0603_1608Metric
- C909: renamed from C910; footprint Capacitor_SMD:C_0805_2012Metric -> Capacitor_SMD:C_0603_1608Metric
- C910: renamed from C911; footprint Capacitor_SMD:C_0805_2012Metric -> Capacitor_SMD:C_0603_1608Metric
- C911: renamed from C912; footprint Capacitor_SMD:C_0805_2012Metric -> Capacitor_SMD:C_0603_1608Metric
- R1001, R1002, R1003, R1004, R101, R106, R107, R108, R109, R1101, R1102, R1103, R1104, R1201, R1202, R1203, R1204, R1301, R1302, R1303, R1304, R1401, R1402, R1403, R1404, R1501, R1502, R1503, R1504, R1601, R1602, R1603, R1604, R1701, R1702, R1703, R1704, R1801, R1802, R1803, R1804, R1901, R1902, R1903, R1904, R201, R301, R302, R303, R304, R305, R306, R307, R308, R309, R310, R311, R312, R401, R402, R403, R404, R501, R502, R503, R504, R601, R602, R603, R604, R701, R702, R703, R704, R801, R901: footprint Resistor_SMD:R_0805_2012Metric -> Resistor_SMD:R_0603_1608Metric
- R102: renamed from R104; footprint Resistor_SMD:R_0805_2012Metric -> Resistor_SMD:R_0603_1608Metric
- R103: renamed from R105; footprint Resistor_SMD:R_0805_2012Metric -> Resistor_SMD:R_0603_1608Metric
- R104: renamed from R110; footprint Resistor_SMD:R_0805_2012Metric -> Resistor_SMD:R_0603_1608Metric
- R105: renamed from R111; footprint Resistor_SMD:R_0805_2012Metric -> Resistor_SMD:R_0603_1608Metric
- R110: renamed from R102; footprint Resistor_SMD:R_0805_2012Metric -> Resistor_SMD:R_0603_1608Metric
- R111: renamed from R103; footprint Resistor_SMD:R_0805_2012Metric -> Resistor_SMD:R_0603_1608Metric
- R202: renamed from R203; footprint Resistor_SMD:R_0805_2012Metric -> Resistor_SMD:R_0603_1608Metric
- R203: renamed from R202; footprint Resistor_SMD:R_0805_2012Metric -> Resistor_SMD:R_0603_1608Metric
- R204: renamed from R205; footprint Resistor_SMD:R_0805_2012Metric -> Resistor_SMD:R_0603_1608Metric
- R205: renamed from R206; footprint Resistor_SMD:R_0805_2012Metric -> Resistor_SMD:R_0603_1608Metric
- R206: renamed from R207; footprint Resistor_SMD:R_0805_2012Metric -> Resistor_SMD:R_0603_1608Metric
- R207: renamed from R208; footprint Resistor_SMD:R_0805_2012Metric -> Resistor_SMD:R_0603_1608Metric
- R208: renamed from R209; footprint Resistor_SMD:R_0805_2012Metric -> Resistor_SMD:R_0603_1608Metric
- R209: renamed from R210; footprint Resistor_SMD:R_0805_2012Metric -> Resistor_SMD:R_0603_1608Metric
- R210: renamed from R212; footprint Resistor_SMD:R_0805_2012Metric -> Resistor_SMD:R_0603_1608Metric
- R802: renamed from R803; footprint Resistor_SMD:R_0805_2012Metric -> Resistor_SMD:R_0603_1608Metric
- R803: renamed from R802; footprint Resistor_SMD:R_0805_2012Metric -> Resistor_SMD:R_0603_1608Metric
- R804: renamed from R807; footprint Resistor_SMD:R_0805_2012Metric -> Resistor_SMD:R_0603_1608Metric
- R805: renamed from R806; footprint Resistor_SMD:R_0805_2012Metric -> Resistor_SMD:R_0603_1608Metric
- R806: renamed from R804; footprint Resistor_SMD:R_0805_2012Metric -> Resistor_SMD:R_0603_1608Metric
- R807: renamed from R805; footprint Resistor_SMD:R_0805_2012Metric -> Resistor_SMD:R_0603_1608Metric
- R902: value 100 -> 330K; footprint Resistor_SMD:R_0805_2012Metric -> Resistor_SMD:R_0603_1608Metric
- R903: value 100 -> 33K; footprint Resistor_SMD:R_0805_2012Metric -> Resistor_SMD:R_0603_1608Metric
- R904: value 100 -> 1M; footprint Resistor_SMD:R_0805_2012Metric -> Resistor_SMD:R_0603_1608Metric
- R905: value 100 -> 2.2M; footprint Resistor_SMD:R_0805_2012Metric -> Resistor_SMD:R_0603_1608Metric
- moved R902 228.0 mm to (120.4, 85.2)
- moved R903 227.8 mm to (120.4, 89.2), turned to -90 degrees
- moved R905 227.6 mm to (118.9, 89.2), turned to -90 degrees
- moved R904 224.9 mm to (116.7, 88.5)
- moved C904 200.4 mm to (97.8, 96.7)
- moved C910 182.9 mm to (89.4, 96.6)
- moved R1704 181.6 mm to (90.1, 100.4), turned to 90 degrees
- moved R1703 180.8 mm to (89.5, 98.1)
- moved C905 178.3 mm to (81.4, 96.6)
- moved R1702 176.9 mm to (86.4, 98.1)
- moved R1701 176.5 mm to (86.4, 96.6)
- moved R901 176.0 mm to (69.9, 95.2)
- moved Q1701 172.1 mm to (87.6, 100.8), turned to -90 degrees
- moved C911 167.5 mm to (72.9, 96.7)
- moved R1804 163.4 mm to (81.9, 100.3), turned to 90 degrees
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- renumbered C202 to C203, C208 to C209, D802 to D801, D801 to D802, H115 to H114, H114 to H115, U804 to U803
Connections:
- C903 pad 1: /CB Mosfets/VC4 -> /CB Mosfets/VC5
- C903 pad 2: /CB Mosfets/VC3 -> /CB Mosfets/VC4
- C904 pad 1: /CB Mosfets/VC6 -> /CB Mosfets/VC7
- C904 pad 2: /CB Mosfets/VC5 -> /CB Mosfets/VC6
- C905 pad 1: /CB Mosfets/VC8 -> /CB Mosfets/VC9
- C905 pad 2: /CB Mosfets/VC7 -> /CB Mosfets/VC8
- C908 pad 1: /CB Mosfets/VC3 -> /CB Mosfets/VC4
- C908 pad 2: /CB Mosfets/VC2 -> /CB Mosfets/VC3
- C909 pad 1: /CB Mosfets/VC5 -> /CB Mosfets/VC6
- C909 pad 2: /CB Mosfets/VC4 -> /CB Mosfets/VC5
- C910 pad 1: /CB Mosfets/VC7 -> /CB Mosfets/VC8
- C910 pad 2: /CB Mosfets/VC6 -> /CB Mosfets/VC7
- C911 pad 1: /CB Mosfets/VC9 -> /CB Mosfets/VC10
- C911 pad 2: /CB Mosfets/VC8 -> /CB Mosfets/VC9
- Q1301 pad 2: /CB Mosfets/CELL2 -> /CB Mosfets/CELL3
- Q1401 pad 2: /CB Mosfets/CELL3 -> /CB Mosfets/CELL4
- Q1501 pad 2: /CB Mosfets/CELL4 -> /CB Mosfets/CELL5
- Q1601 pad 2: /CB Mosfets/CELL5 -> /CB Mosfets/CELL6
- Q1701 pad 2: /CB Mosfets/CELL6 -> /CB Mosfets/CELL7
- Q1801 pad 2: /CB Mosfets/CELL7 -> /CB Mosfets/CELL8
- Q1901 pad 2: /CB Mosfets/CELL8 -> /CB Mosfets/CELL9
- R1301 pad 1: /CB Mosfets/CELL3 -> /CB Mosfets/CELL4
- R1302 pad 1: /CB Mosfets/CELL3 -> /CB Mosfets/CELL4
- R1303 pad 2: /CB Mosfets/VC2 -> /CB Mosfets/VC3
- R1304 pad 1: /CB Mosfets/CELL2 -> /CB Mosfets/CELL3
- R1304 pad 2: /CB Mosfets/VC2 -> /CB Mosfets/VC3
- R1401 pad 1: /CB Mosfets/CELL4 -> /CB Mosfets/CELL5
- R1402 pad 1: /CB Mosfets/CELL4 -> /CB Mosfets/CELL5
- R1403 pad 2: /CB Mosfets/VC3 -> /CB Mosfets/VC4
- R1404 pad 1: /CB Mosfets/CELL3 -> /CB Mosfets/CELL4
- R1404 pad 2: /CB Mosfets/VC3 -> /CB Mosfets/VC4
- R1501 pad 1: /CB Mosfets/CELL5 -> /CB Mosfets/CELL6
- R1502 pad 1: /CB Mosfets/CELL5 -> /CB Mosfets/CELL6
- R1503 pad 2: /CB Mosfets/VC4 -> /CB Mosfets/VC5
- R1504 pad 1: /CB Mosfets/CELL4 -> /CB Mosfets/CELL5
- R1504 pad 2: /CB Mosfets/VC4 -> /CB Mosfets/VC5
- R1601 pad 1: /CB Mosfets/CELL6 -> /CB Mosfets/CELL7
- R1602 pad 1: /CB Mosfets/CELL6 -> /CB Mosfets/CELL7
- R1603 pad 2: /CB Mosfets/VC5 -> /CB Mosfets/VC6
- R1604 pad 1: /CB Mosfets/CELL5 -> /CB Mosfets/CELL6
- R1604 pad 2: /CB Mosfets/VC5 -> /CB Mosfets/VC6
- R1701 pad 1: /CB Mosfets/CELL7 -> /CB Mosfets/CELL8
- R1702 pad 1: /CB Mosfets/CELL7 -> /CB Mosfets/CELL8
- R1703 pad 2: /CB Mosfets/VC6 -> /CB Mosfets/VC7
- R1704 pad 1: /CB Mosfets/CELL6 -> /CB Mosfets/CELL7
- R1704 pad 2: /CB Mosfets/VC6 -> /CB Mosfets/VC7
- R1801 pad 1: /CB Mosfets/CELL8 -> /CB Mosfets/CELL9
- R1802 pad 1: /CB Mosfets/CELL8 -> /CB Mosfets/CELL9
- R1803 pad 2: /CB Mosfets/VC7 -> /CB Mosfets/VC8
- R1804 pad 1: /CB Mosfets/CELL7 -> /CB Mosfets/CELL8
- R1804 pad 2: /CB Mosfets/VC7 -> /CB Mosfets/VC8
- R1901 pad 1: /CB Mosfets/CELL9 -> /CB Mosfets/CELL10
- R1902 pad 1: /CB Mosfets/CELL9 -> /CB Mosfets/CELL10
- R1903 pad 2: /CB Mosfets/VC8 -> /CB Mosfets/VC9
- R1904 pad 1: /CB Mosfets/CELL8 -> /CB Mosfets/CELL9
- R1904 pad 2: /CB Mosfets/VC8 -> /CB Mosfets/VC9
